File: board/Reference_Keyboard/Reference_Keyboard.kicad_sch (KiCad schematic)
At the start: 76 parts, among them J1 Conn_01x03_Pin, J2 USB_C_Receptacle_USB2.0, J3 Conn_01x04_Pin, J4 84953-4, SW1 SW_Push, SW10 SW_Push, SW11 SW_Push, SW12 SW_Push, SW13 SW_Push, SW14 SW_Push, SW15 SW_Push, SW16 SW_Push, SW17 SW_Push, SW18 SW_Push, SW19 SW_Push, SW2 SW_Push, SW20 SW_Push, SW21 SW_Push, SW22 SKQGAFE010, SW23 SKQGAFE010, SW24 RotaryEncoder_Switch, SW3 SW_Push, SW4 SW_Push, SW5 SW_Push, SW6 SW_Push, SW7 SW_Push, SW8 SW_Push, SW9 SW_Push, U1 RP2040, U2 W25Q16JVSSIM, U3 LM1117RS-3.3, Y1 NX3225SA-12MHz-STD-CSR-6

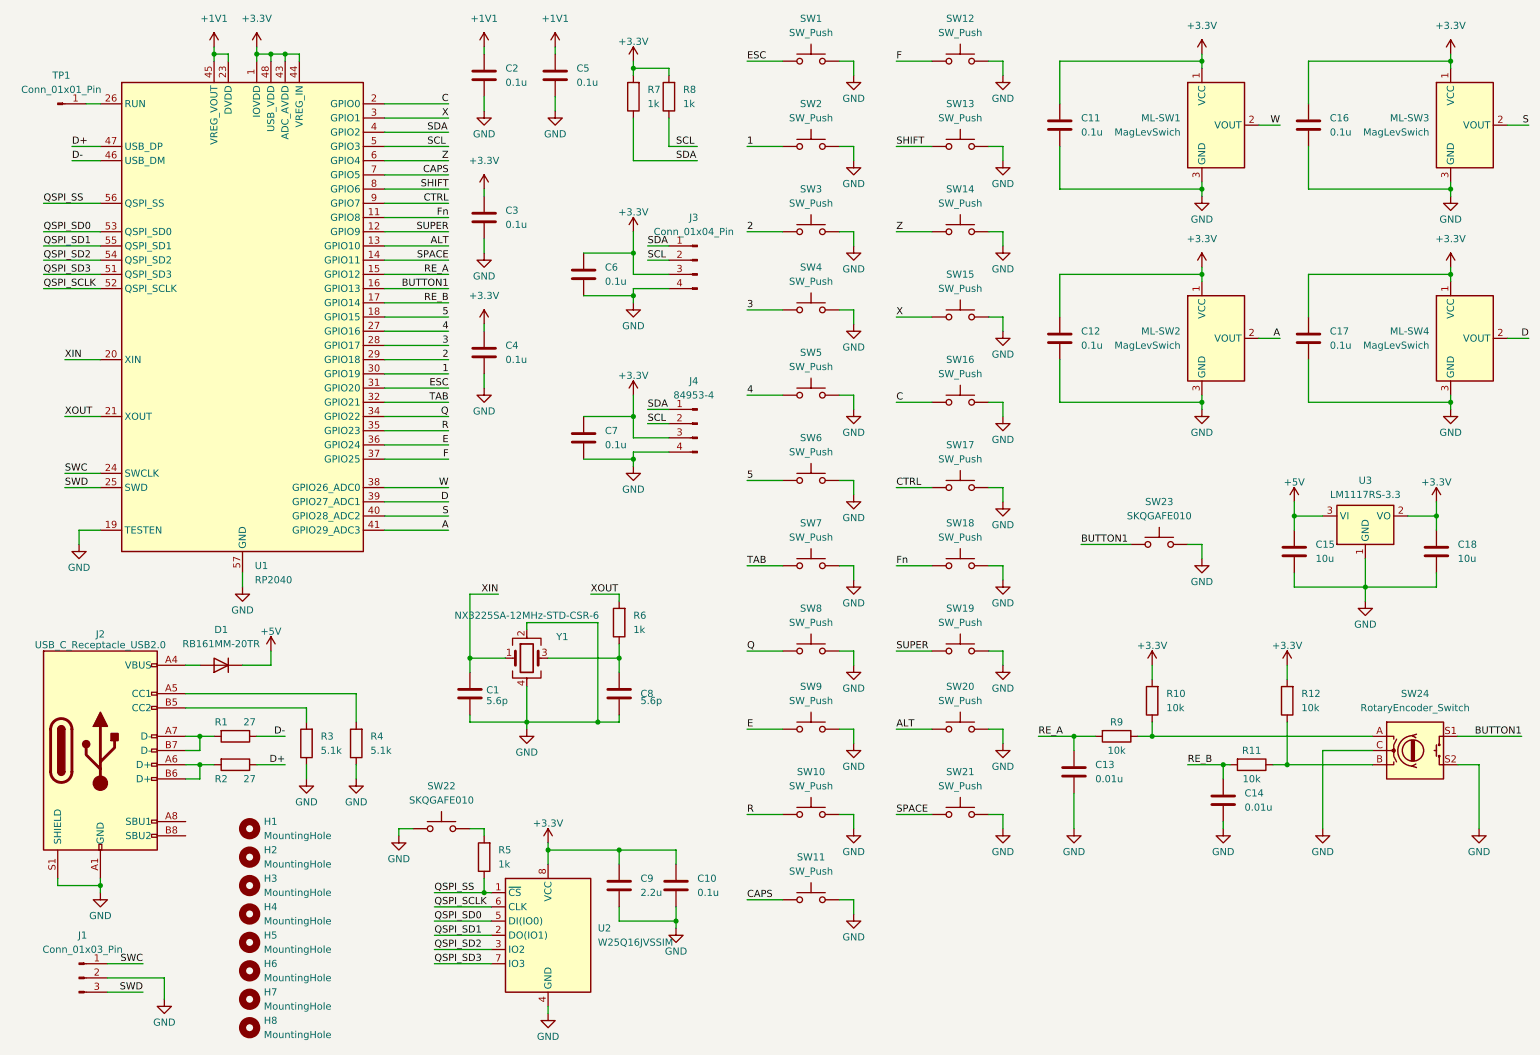
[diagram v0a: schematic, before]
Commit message: Bug fix for the Fn key
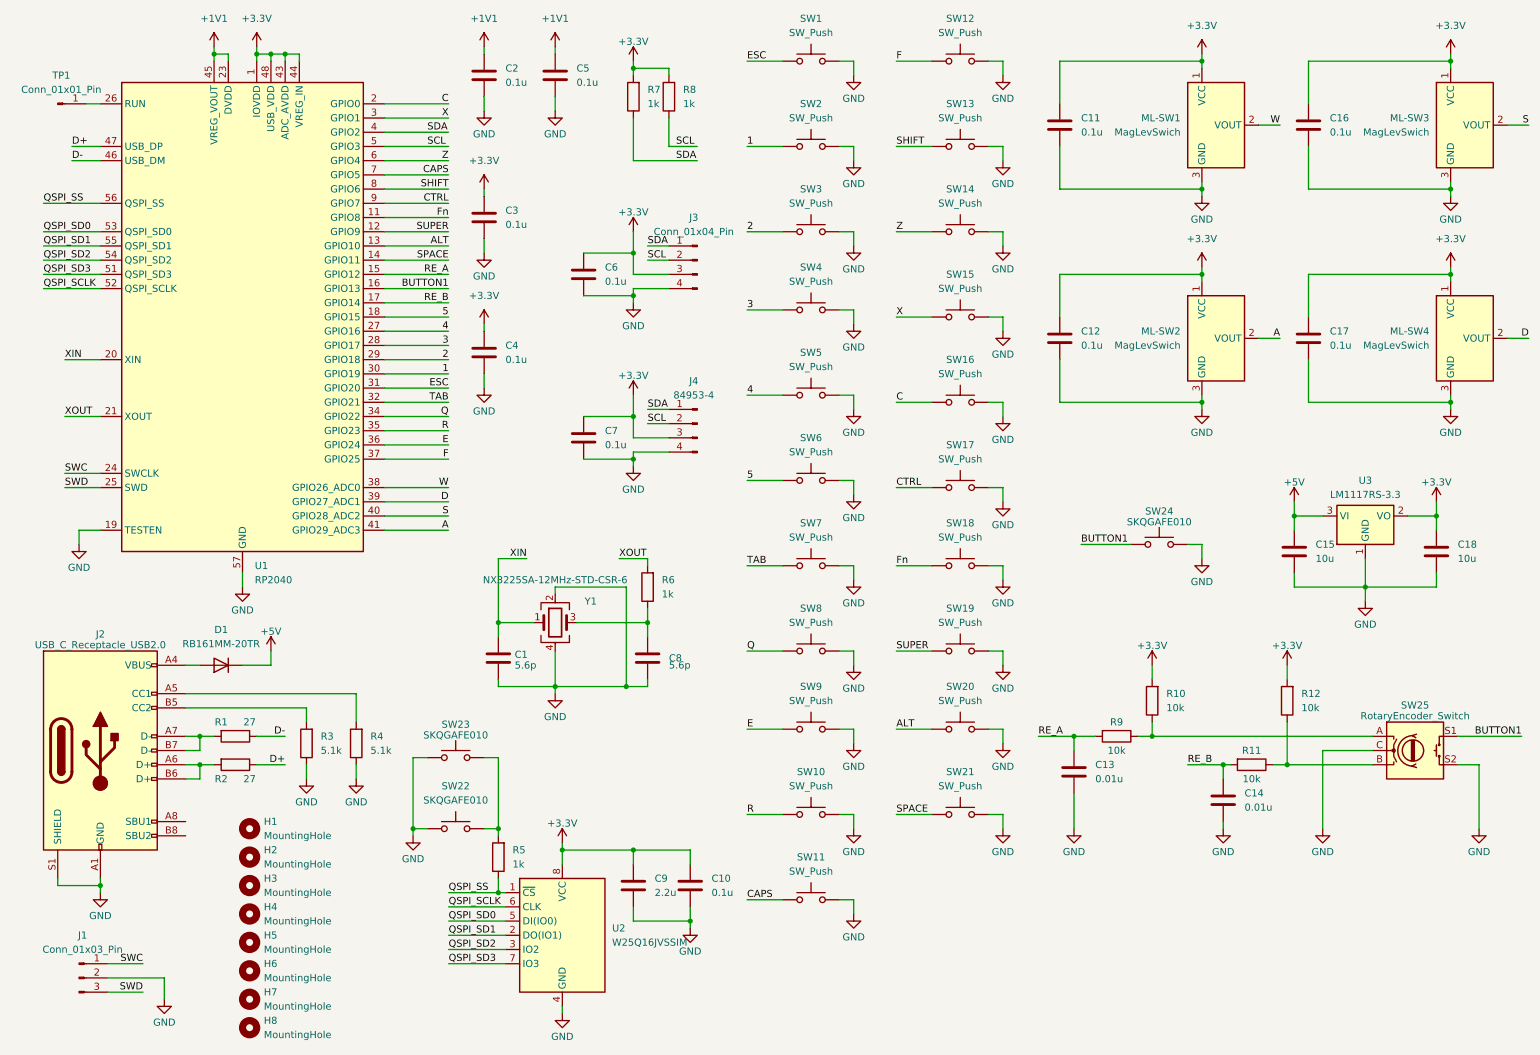
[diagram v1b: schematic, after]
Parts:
- added SW23: SKQGAFE010, Button_Switch_SMD:SW_SPST_SKQG_WithStem, symbol Switch:SW_Push
- renumbered SW23 to SW24, SW24 to SW25
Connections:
- net GND: now also SW23.1
- net at R5.2, SW22.2: now also SW23.2
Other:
- moved on the sheet: C1, C10, C8, C9, R5, R6, SW22, U2, Y1
